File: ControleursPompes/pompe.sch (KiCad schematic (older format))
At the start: 9 parts, among them J6 PV, J7 EV, J8 VACUOSTAT, U3 TB6612FNG

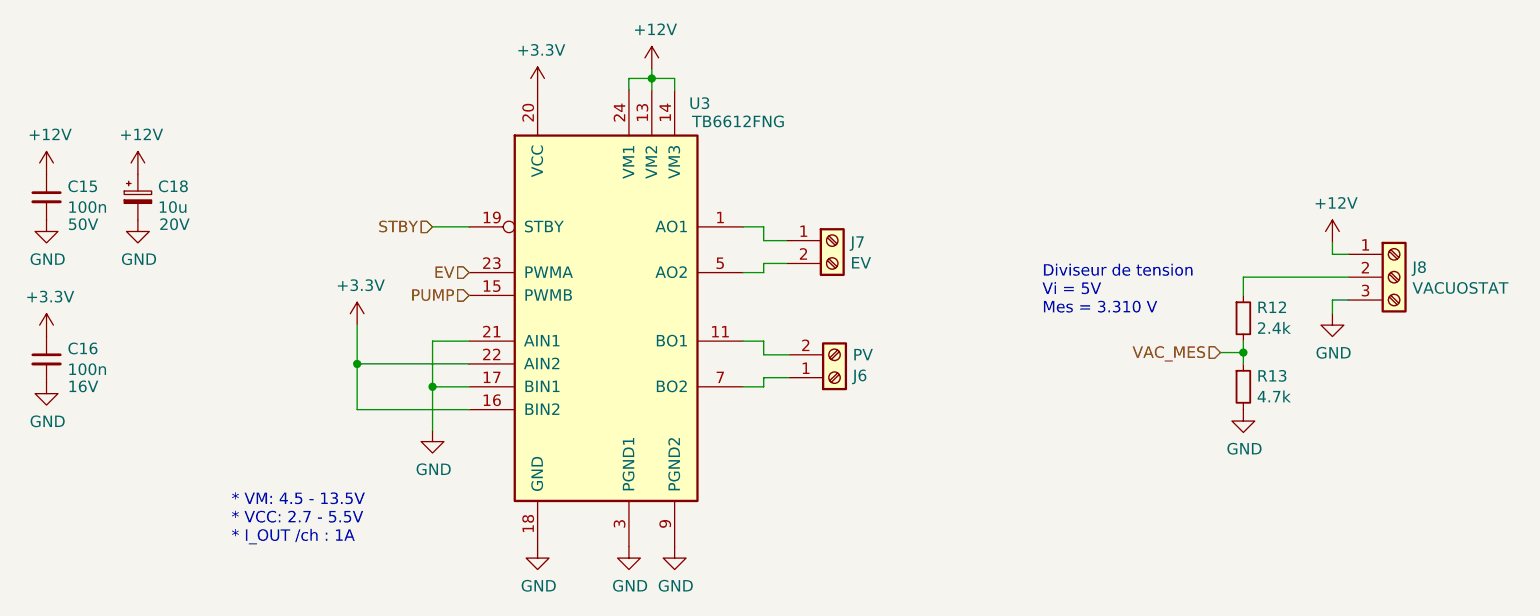
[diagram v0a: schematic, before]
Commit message: Ajout bornier alim 5V sur controleur pompes
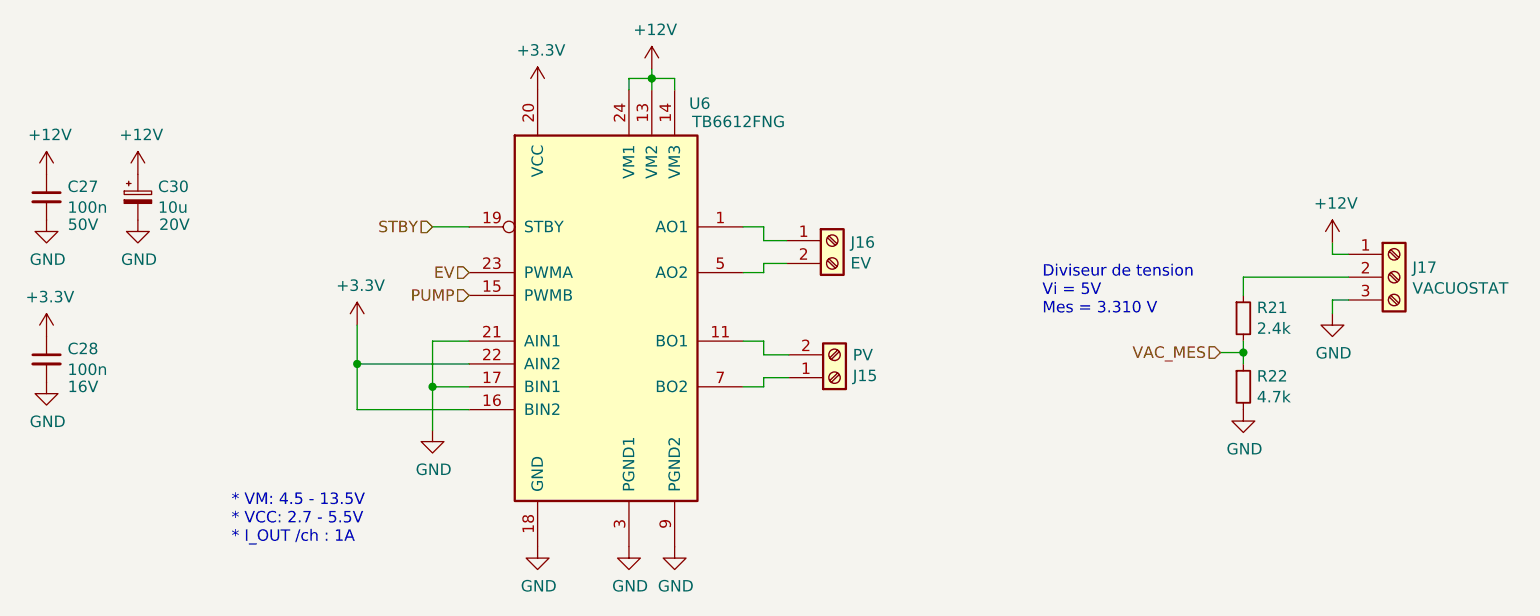
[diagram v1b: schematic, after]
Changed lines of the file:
@@
 AR Path="/60645D35/60396CF3" Ref="U5"  Part="1"
 AR Path="/6064B8C7/60396CF3" Ref="U6"  Part="1"
-F 0 "U3" H 5600 4380 50  0000 C CNN
+F 0 "U6" H 5600 4380 50  0000 C CNN
 F 1 "TB6612FNG" H 5770 4300 50  0000 C CNN
 F 2 "Package_SO:SSOP-24_5.3x8.2mm_P0.65mm" H 6490 2540 50  0001 C CNN
@@
 AR Path="/60645D35/6039833C" Ref="#PWR0101"  Part="1"
 AR Path="/6064B8C7/6039833C" Ref="#PWR0120"  Part="1"
-F 0 "#PWR063" H 4890 4190 50  0001 C CNN
+F 0 "#PWR0120" H 4890 4190 50  0001 C CNN
 F 1 "GND" H 4895 4267 50  0000 C CNN
 F 2 "" H 4890 4440 50  0001 C CNN
@@
 AR Path="/60645D35/60399A93" Ref="#PWR0102"  Part="1"
 AR Path="/6064B8C7/60399A93" Ref="#PWR0121"  Part="1"
-F 0 "#PWR064" H 5290 4190 50  0001 C CNN
+F 0 "#PWR0121" H 5290 4190 50  0001 C CNN
 F 1 "GND" H 5295 4267 50  0000 C CNN
 F 2 "" H 5290 4440 50  0001 C CNN
@@
 AR Path="/60645D35/60399EC1" Ref="#PWR0104"  Part="1"
 AR Path="/6064B8C7/60399EC1" Ref="#PWR0123"  Part="1"
-F 0 "#PWR066" H 5490 4190 50  0001 C CNN
+F 0 "#PWR0123" H 5490 4190 50  0001 C CNN
 F 1 "GND" H 5495 4267 50  0000 C CNN
 F 2 "" H 5490 4440 50  0001 C CNN
@@
 AR Path="/60645D35/6039B34D" Ref="J13"  Part="1"
 AR Path="/6064B8C7/6039B34D" Ref="J16"  Part="1"
-F 0 "J7" H 6260 3092 50  0000 L CNN
+F 0 "J16" H 6260 3092 50  0000 L CNN
 F 1 "EV" H 6260 3001 50  0000 L CNN
 F 2 "TerminalBlock_Phoenix:TerminalBlock_Phoenix_MPT-0,5-2-2.54_1x02_P2.54mm_Horizontal" H 6180 3100 50  0001 C CNN
@@
 AR Path="/60645D35/6039C299" Ref="J12"  Part="1"
 AR Path="/6064B8C7/6039C299" Ref="J15"  Part="1"
-F 0 "J6" H 6270 3692 50  0000 L CNN
+F 0 "J15" H 6270 3692 50  0000 L CNN
 F 1 "PV" H 6270 3601 50  0000 L CNN
 F 2 "TerminalBlock_Phoenix:TerminalBlock_Phoenix_MPT-0,5-2-2.54_1x02_P2.54mm_Horizontal" H 6190 3700 50  0001 C CNN
@@
 AR Path="/60645D35/603A39B0" Ref="#PWR0100"  Part="1"
 AR Path="/6064B8C7/603A39B0" Ref="#PWR0119"  Part="1"
-F 0 "#PWR062" H 4890 2290 50  0001 C CNN
+F 0 "#PWR0119" H 4890 2290 50  0001 C CNN
 F 1 "+3.3V" H 4905 2613 50  0000 C CNN
 F 2 "" H 4890 2440 50  0001 C CNN
@@
 AR Path="/60645D35/603A4753" Ref="#PWR091"  Part="1"
 AR Path="/6064B8C7/603A4753" Ref="#PWR0110"  Part="1"
-F 0 "#PWR053" H 2740 3370 50  0001 C CNN
+F 0 "#PWR0110" H 2740 3370 50  0001 C CNN
 F 1 "+3.3V" H 2755 3693 50  0000 C CNN
 F 2 "" H 2740 3520 50  0001 C CNN
@@
 AR Path="/60645D35/603A5013" Ref="#PWR092"  Part="1"
 AR Path="/6064B8C7/603A5013" Ref="#PWR0111"  Part="1"
-F 0 "#PWR054" H 2740 3470 50  0001 C CNN
+F 0 "#PWR0111" H 2740 3470 50  0001 C CNN
 F 1 "GND" H 2745 3547 50  0000 C CNN
 F 2 "" H 2740 3720 50  0001 C CNN
@@
 AR Path="/60645D35/603A6134" Ref="C24"  Part="1"
 AR Path="/6064B8C7/603A6134" Ref="C28"  Part="1"
-F 0 "C16" H 2832 3666 50  0000 L CNN
+F 0 "C28" H 2832 3666 50  0000 L CNN
 F 1 "100n" H 2832 3575 50  0000 L CNN
 F 2 "Capacitor_SMD:C_0402_1005Metric_Pad0.74x0.62mm_HandSolder" H 2740 3620 50  0001 C CNN
@@
 AR Path="/60645D35/603B9B29" Ref="C23"  Part="1"
 AR Path="/6064B8C7/603B9B29" Ref="C27"  Part="1"
-F 0 "C15" H 2832 2956 50  0000 L CNN
+F 0 "C27" H 2832 2956 50  0000 L CNN
 F 1 "100n" H 2832 2865 50  0000 L CNN
 F 2 "Capacitor_SMD:C_0805_2012Metric_Pad1.18x1.45mm_HandSolder" H 2740 2910 50  0001 C CNN
@@
 AR Path="/60645D35/603BF46B" Ref="#PWR090"  Part="1"
 AR Path="/6064B8C7/603BF46B" Ref="#PWR0109"  Part="1"
-F 0 "#PWR052" H 2740 2760 50  0001 C CNN
+F 0 "#PWR0109" H 2740 2760 50  0001 C CNN
 F 1 "GND" H 2745 2837 50  0000 C CNN
 F 2 "" H 2740 3010 50  0001 C CNN
@@
 AR Path="/60645D35/603C59D7" Ref="J14"  Part="1"
 AR Path="/6064B8C7/603C59D7" Ref="J17"  Part="1"
-F 0 "J8" H 8720 3302 50  0000 L CNN
+F 0 "J17" H 8720 3302 50  0000 L CNN
 F 1 "VACUOSTAT" H 8720 3211 50  0000 L CNN
 F 2 "TerminalBlock_Phoenix:TerminalBlock_Phoenix_MPT-0,5-3-2.54_1x03_P2.54mm_Horizontal" H 8640 3260 50  0001 C CNN
@@
 AR Path="/60645D35/603C78D7" Ref="#PWR0107"  Part="1"
 AR Path="/6064B8C7/603C78D7" Ref="#PWR0126"  Part="1"
-F 0 "#PWR069" H 8370 3170 50  0001 C CNN
+F 0 "#PWR0126" H 8370 3170 50  0001 C CNN
 F 1 "GND" H 8375 3247 50  0000 C CNN
 F 2 "" H 8370 3420 50  0001 C CNN
@@
 AR Path="/60645D35/603D5A20" Ref="C26"  Part="1"
 AR Path="/6064B8C7/603D5A20" Ref="C30"  Part="1"
-F 0 "C18" H 3228 2956 50  0000 L CNN
+F 0 "C30" H 3228 2956 50  0000 L CNN
 F 1 "10u" H 3228 2865 50  0000 L CNN
 F 2 "Capacitor_Tantalum_SMD:CP_EIA-3528-21_Kemet-B_Pad1.50x2.35mm_HandSolder" H 3140 2910 50  0001 C CNN
@@
 AR Path="/60645D35/603D9377" Ref="#PWR096"  Part="1"
 AR Path="/6064B8C7/603D9377" Ref="#PWR0115"  Part="1"
-F 0 "#PWR058" H 3140 2760 50  0001 C CNN
+F 0 "#PWR0115" H 3140 2760 50  0001 C CNN
 F 1 "GND" H 3145 2837 50  0000 C CNN
 F 2 "" H 3140 3010 50  0001 C CNN
@@
 AR Path="/60645D35/603E6B46" Ref="R18"  Part="1"
 AR Path="/6064B8C7/603E6B46" Ref="R21"  Part="1"
-F 0 "R12" H 8039 3486 50  0000 L CNN
+F 0 "R21" H 8039 3486 50  0000 L CNN
 F 1 "2.4k" H 8039 3395 50  0000 L CNN
 F 2 "Resistor_SMD:R_0805_2012Metric_Pad1.20x1.40mm_HandSolder" H 7980 3440 50  0001 C CNN
@@
 AR Path="/60645D35/603E8F6F" Ref="R19"  Part="1"
 AR Path="/6064B8C7/603E8F6F" Ref="R22"  Part="1"
-F 0 "R13" H 8039 3786 50  0000 L CNN
+F 0 "R22" H 8039 3786 50  0000 L CNN
 F 1 "4.7k" H 8039 3695 50  0000 L CNN
 F 2 "Resistor_SMD:R_0805_2012Metric_Pad1.20x1.40mm_HandSolder" H 7980 3740 50  0001 C CNN
@@
 AR Path="/60645D35/603E9C8B" Ref="#PWR0105"  Part="1"
 AR Path="/6064B8C7/603E9C8B" Ref="#PWR0124"  Part="1"
-F 0 "#PWR067" H 7980 3590 50  0001 C CNN
+F 0 "#PWR0124" H 7980 3590 50  0001 C CNN
 F 1 "GND" H 7985 3667 50  0000 C CNN
 F 2 "" H 7980 3840 50  0001 C CNN
@@
 AR Path="/60645D35/603B3F88" Ref="#PWR0106"  Part="1"
 AR Path="/6064B8C7/603B3F88" Ref="#PWR0125"  Part="1"
-F 0 "#PWR068" H 8370 2960 50  0001 C CNN
+F 0 "#PWR0125" H 8370 2960 50  0001 C CNN
 F 1 "+12V" H 8385 3283 50  0000 C CNN
 F 2 "" H 8370 3110 50  0001 C CNN
@@
 AR Path="/60645D35/603B6BAE" Ref="#PWR0103"  Part="1"
 AR Path="/6064B8C7/603B6BAE" Ref="#PWR0122"  Part="1"
-F 0 "#PWR065" H 5390 2200 50  0001 C CNN
+F 0 "#PWR0122" H 5390 2200 50  0001 C CNN
 F 1 "+12V" H 5405 2523 50  0000 C CNN
 F 2 "" H 5390 2350 50  0001 C CNN
@@
 AR Path="/60645D35/603B7FD5" Ref="#PWR089"  Part="1"
 AR Path="/6064B8C7/603B7FD5" Ref="#PWR0108"  Part="1"
-F 0 "#PWR051" H 2740 2660 50  0001 C CNN
+F 0 "#PWR0108" H 2740 2660 50  0001 C CNN
 F 1 "+12V" H 2755 2983 50  0000 C CNN
 F 2 "" H 2740 2810 50  0001 C CNN
@@
 AR Path="/60645D35/603BA293" Ref="#PWR095"  Part="1"
 AR Path="/6064B8C7/603BA293" Ref="#PWR0114"  Part="1"
-F 0 "#PWR057" H 3140 2660 50  0001 C CNN
+F 0 "#PWR0114" H 3140 2660 50  0001 C CNN
 F 1 "+12V" H 3155 2983 50  0000 C CNN
 F 2 "" H 3140 2810 50  0001 C CNN
@@
 AR Path="/60645D35/605A9B9D" Ref="#PWR098"  Part="1"
 AR Path="/6064B8C7/605A9B9D" Ref="#PWR0117"  Part="1"
-F 0 "#PWR060" H 4430 3680 50  0001 C CNN
+F 0 "#PWR0117" H 4430 3680 50  0001 C CNN
 F 1 "GND" H 4435 3757 50  0000 C CNN
 F 2 "" H 4430 3930 50  0001 C CNN
@@
 AR Path="/60645D35/605AAAC5" Ref="#PWR097"  Part="1"
 AR Path="/6064B8C7/605AAAC5" Ref="#PWR0116"  Part="1"
-F 0 "#PWR059" H 4100 3320 50  0001 C CNN
+F 0 "#PWR0116" H 4100 3320 50  0001 C CNN
 F 1 "+3.3V" H 4115 3643 50  0000 C CNN
 F 2 "" H 4100 3470 50  0001 C CNN
